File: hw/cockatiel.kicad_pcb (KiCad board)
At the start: 4 copper layers, 51 x 60 mm, 39 parts, among them J1 Programmer, J10 MIC_N_BYP, J11 MIC_P_SEL, J12 MIC_N_SEL, J13 Cox Box Mic In, J14 Cox Box Mic Out, J15 Mic Out, J16 Headset/Mic In, J3 DEBUG_UART, J4 RESET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

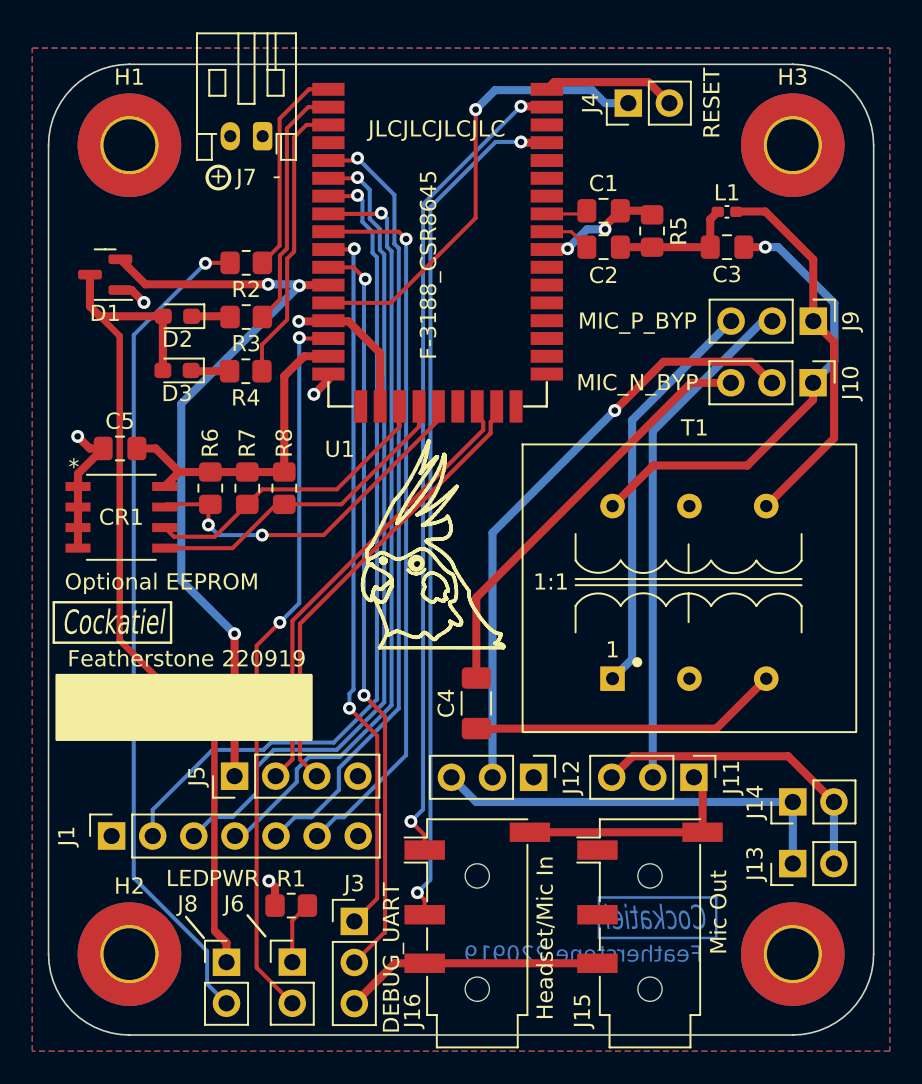
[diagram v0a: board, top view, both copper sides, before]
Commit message: Remove the 'optional' EEPROM
The module already has EEPROM fitted. Removing this simplifies board
layout and size, which will come in handy in the future.
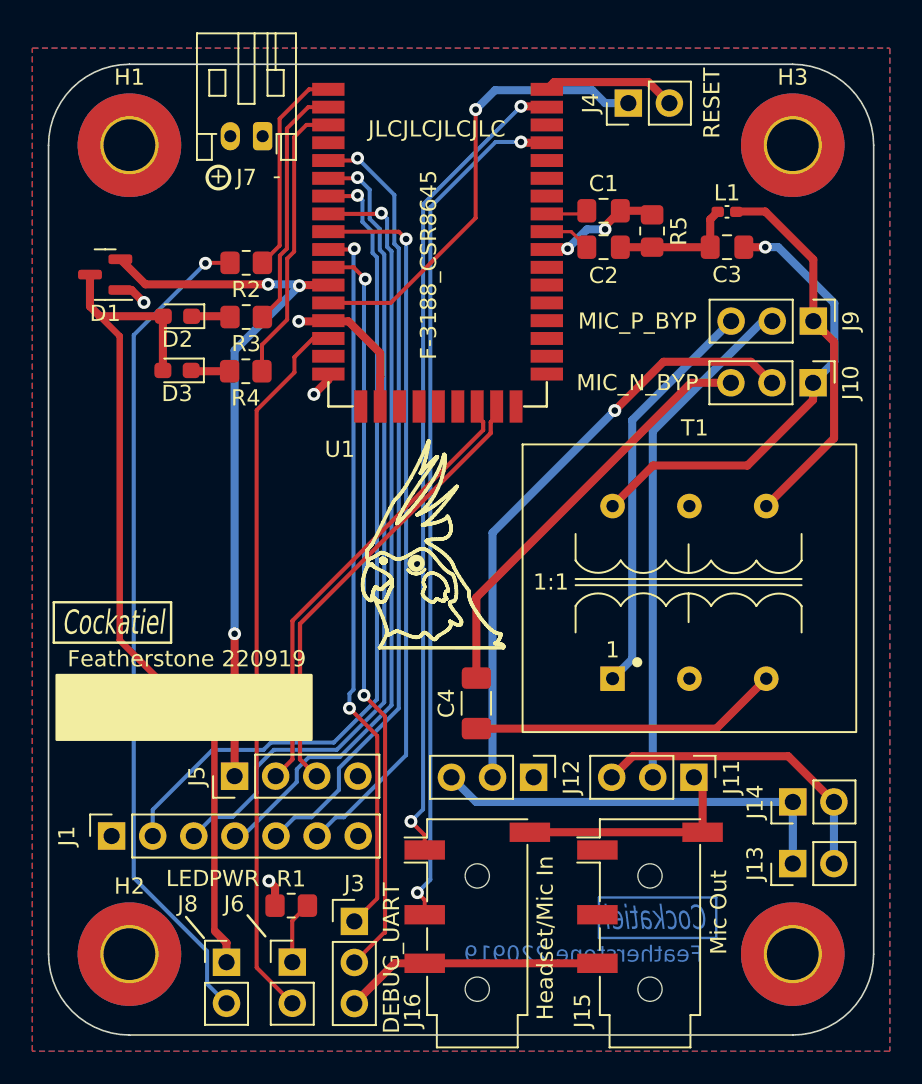
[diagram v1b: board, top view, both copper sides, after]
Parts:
- removed C5: 100n, Capacitor_SMD:C_0805_2012Metric_Pad1.18x1.45mm_HandSolder
- removed CR1: Optional EEPROM, st:M24512-RMN6P
- removed R6, R7, R8: 2K2, Resistor_SMD:R_0805_2012Metric_Pad1.20x1.40mm_HandSolder
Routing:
- net /PIO12: track 22.5 -> 0.00 mm, vias 2 -> 0
- net +1V8: track 20.1 -> 0.00 mm
- net /PIO11: track 20.1 -> 0.00 mm
- net /PIO10: track 18.8 -> 0.00 mm
- net Earth: track 34.7 -> 26.0 mm, vias 2 -> 1
- net VBUS: track 48.3 -> 45.5 mm
- net Net-(J11-Pad1): track 14.3 -> 13.5 mm
- net USB_P: track 28.3 -> 27.7 mm
- net USB_N: track 28.3 -> 27.7 mm
- net Net-(J11-Pad2): track 31.6 -> 31.0 mm
- net /POWER_EN: track 45.0 -> 44.4 mm, vias 2 -> 0
